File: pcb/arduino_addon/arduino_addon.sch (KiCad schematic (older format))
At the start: 33 parts, among them P1 AnalogIn, P11 ADC-DO, P12 ADC-DO, P13 ADC-DO, P14 ADC-DO, P15 DO, P16 3V3 ADC REF, P17 BNC, P2 Power, P3 Digital1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

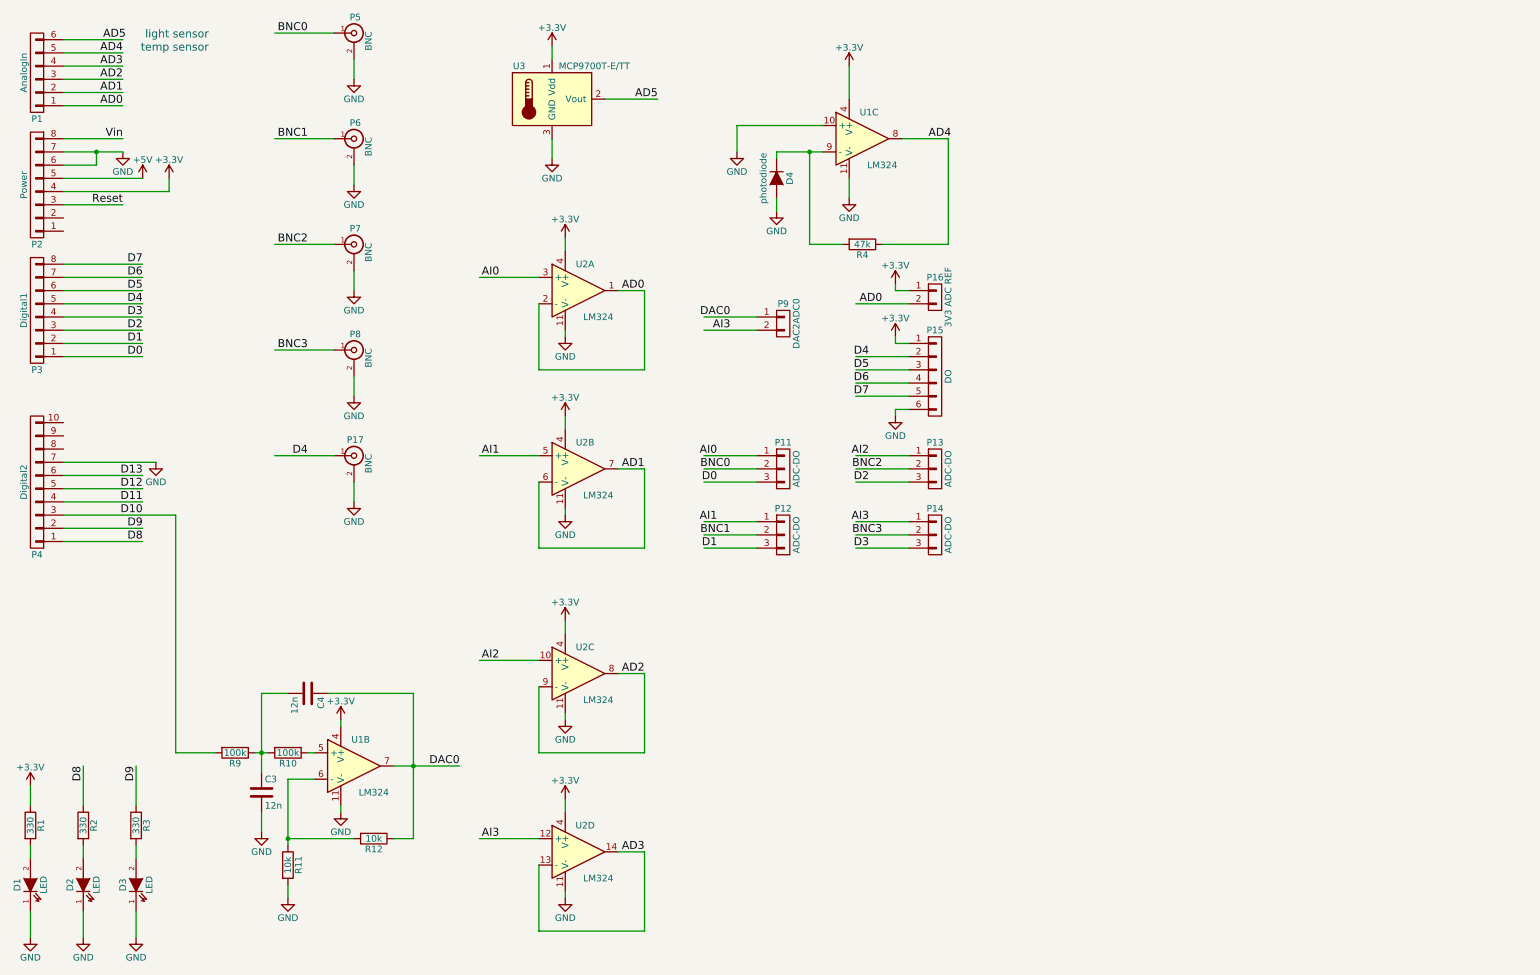
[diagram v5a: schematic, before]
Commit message: Arduino addon V2 is ready, pmt trig generator firmware is updated
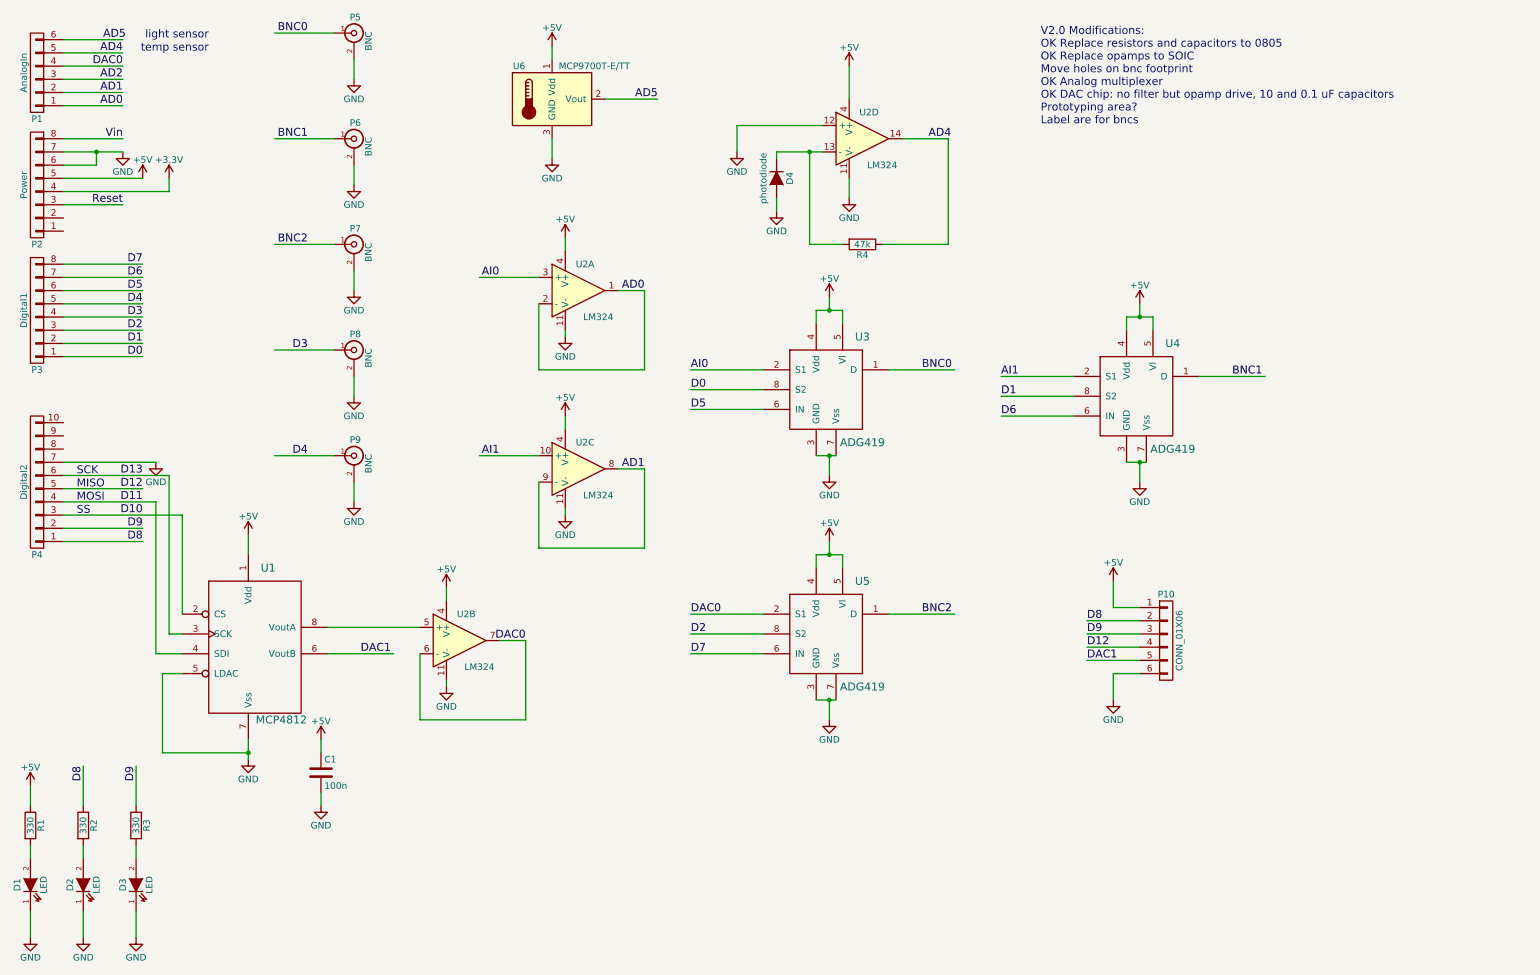
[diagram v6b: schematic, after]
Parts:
- removed C3, C4: 12n, Capacitors_SMD:C_2220_HandSoldering, symbol C
- removed P11, P12, P13, P14: ADC-DO, Pin_Headers:Pin_Header_Straight_1x03, symbol CONN_01X03
- removed P15: DO, Pin_Headers:Pin_Header_Straight_1x06, symbol CONN_01X06
- removed P16: 3V3 ADC REF, Pin_Headers:Pin_Header_Straight_1x02, symbol CONN_01X02
- removed P9: DAC2ADC0, Pin_Headers:Pin_Header_Straight_1x02, symbol CONN_01X02
- removed R10, R9: 100k, Resistors_SMD:R_2512_HandSoldering, symbol R
- removed R11, R12: 10k, Resistors_SMD:R_2512_HandSoldering, symbol R
- removed unit 2 of U1
- removed unit 4 of U2
- added C1: 100n, Capacitors_SMD:C_0805_HandSoldering, symbol C
- added P10: CONN_01X06, Pin_Headers:Pin_Header_Straight_1x06, symbol CONN_01X06
- added U1: MCP4812, Housings_SOIC:SOIC-8_3.9x4.9mm_Pitch1.27mm, symbol MCP4812
- added U3, U4, U5: ADG419, Housings_SOIC:SOIC-8_3.9x4.9mm_Pitch1.27mm, symbol ADG419
- R1, R2, R3: footprint Resistors_SMD:R_2512_HandSoldering -> Resistors_SMD:R_0805_HandSoldering; Part Number 160-20-762 -> 300-56-784
- R4: footprint Resistors_SMD:R_2512_HandSoldering -> Resistors_SMD:R_0805_HandSoldering; Part Number 160-21-026 -> 300-56-806
- U2: renamed from U1; footprint Housings_DIP:DIP-14_W7.62mm_LongPads -> Housings_SOIC:SOIC-14_3.9x8.7mm_Pitch1.27mm; Part Number 173-27-518 -> 173-26-668
- U2: footprint Housings_DIP:DIP-14_W7.62mm_LongPads -> Housings_SOIC:SOIC-14_3.9x8.7mm_Pitch1.27mm; Part Number 173-27-518 -> 173-26-668
- renumbered P17 to P9, U3 to U6
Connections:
- net labels added: DAC1
- net labels removed: AD3, AI2, AI3, BNC3
- wire segments 133 -> 135
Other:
- note added: "MISO"
- note added: "MOSI"
- note added: "SCK"
- note added: "SS"
- note added: "V2.0 Modifications:\nOK Replace resistors and capacitors to 0805\nOK Replace opamps to SOIC\nMove holes on bnc footprint\nOK Analog multiplexer\nOK DAC chip: no filter but opamp drive, 10 and 0.1 uF capacitors\nPrototyping area?\nLabel are for bncs"

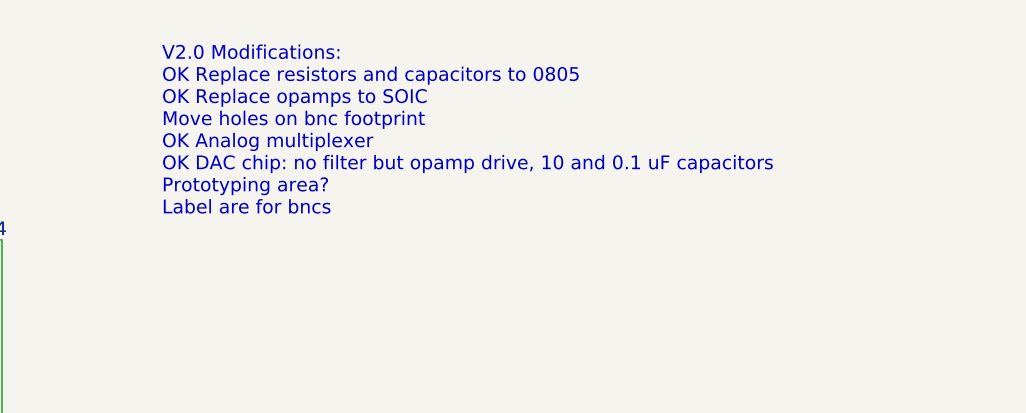
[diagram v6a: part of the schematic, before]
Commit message: addon board bnc connector drill size modification
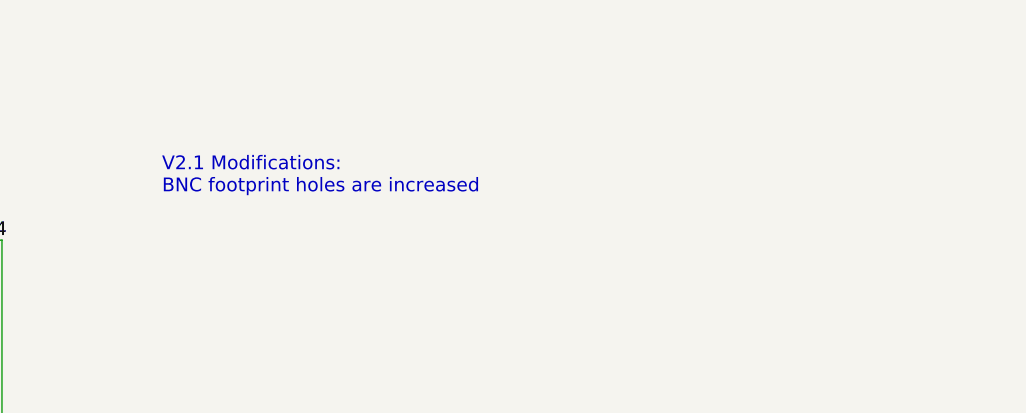
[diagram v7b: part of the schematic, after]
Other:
- note added: "V2.1 Modifications:\nBNC footprint holes are increased\n\n"
- note removed: "V2.0 Modifications:\nOK Replace resistors and capacitors to 0805\nOK Replace opamps to SOIC\nMove holes on bnc footprint\nOK Analog multiplexer\nOK DAC chip: no filter but opamp drive, 10 and 0.1 uF capacitors\nPrototyping area?\nLabel are for bncs"
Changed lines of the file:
@@
 D4
 Text Notes 8500 1400 0    60   ~ 0
-V2.0 Modifications:\nOK Replace resistors and capacitors to 0805\nOK Replace opamps to SOIC\nMove holes on bnc footprint\nOK Analog multiplexer\nOK DAC chip: no filter but opamp drive, 10 and 0.1 uF capacitors\nPrototyping area?\nLabel are for bncs
+V2.1 Modifications:\nBNC footprint holes are increased\n\n
 Text Notes 1200 4050 0    60   ~ 0
 SCK
